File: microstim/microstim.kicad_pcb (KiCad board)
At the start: 2 copper layers, 196.1 x 76.2 mm, 97 parts, among them J1 Conn_Coaxial, J10 Conn_Coaxial, J11 Screw_Terminal_01x02, J12 Conn_Coaxial, J2 Conn_Coaxial, J3 Screw_Terminal_01x02, J4 Screw_Terminal_01x02, J5 Conn_Coaxial, J6 Conn_Coaxial, J7 Screw_Terminal_01x02, J8 Screw_Terminal_01x02, J9 Screw_Terminal_01x02, SW1 SW_Push, SW2 SW_Push, U1 Teensy3.5, U10 AD7321, U11 LTC2057, U12 LTC2057, U13 DG509ACWE, U14 DG509ACWE, U15 LT1167, U16 LT1167, U17 LM358, U18 DG509ACWE, U19 DG509ACWE, U2 CC3-0512DF-E, U3 L78L05_SO8, U4 L78L12_SO8, U5 ISO7760, U6 ISO7760, U7 ISO7341C, U8 L79L12_SO8, U9 MCP4922

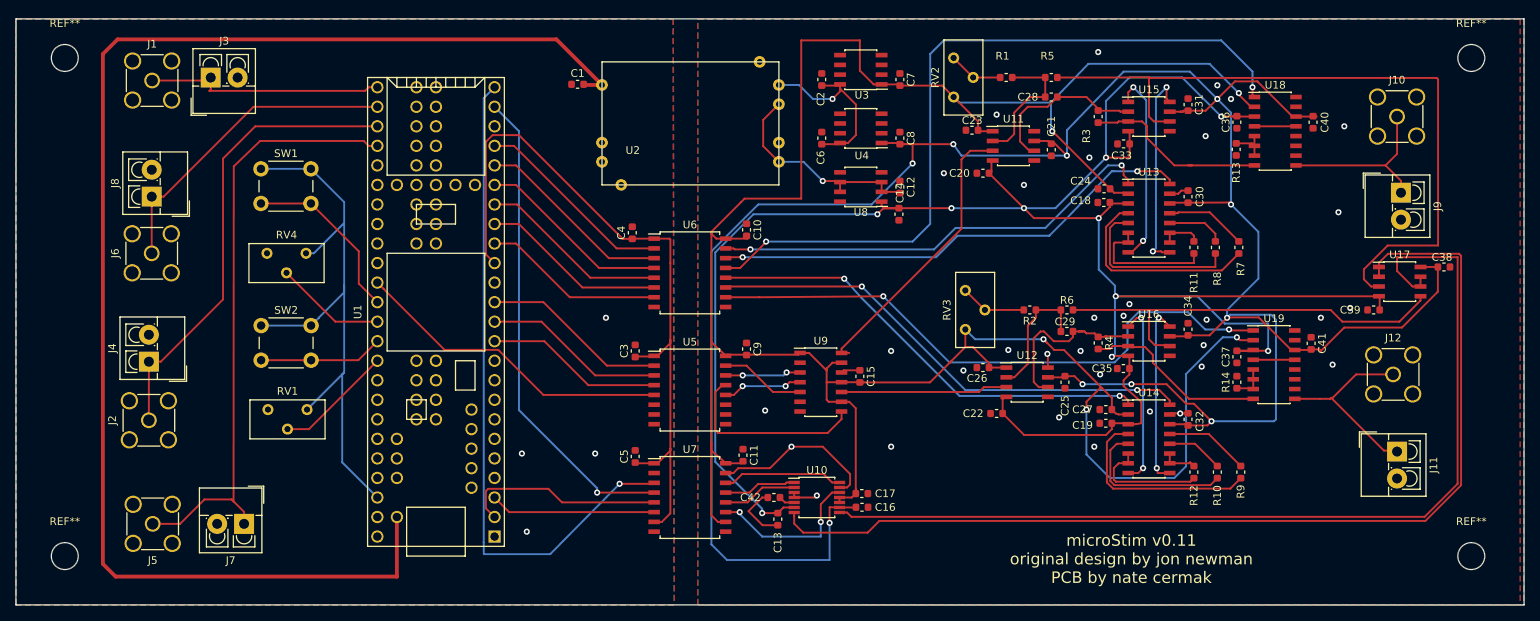
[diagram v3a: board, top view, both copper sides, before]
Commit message: redesign based on improved howland source at jon newmans suggestion
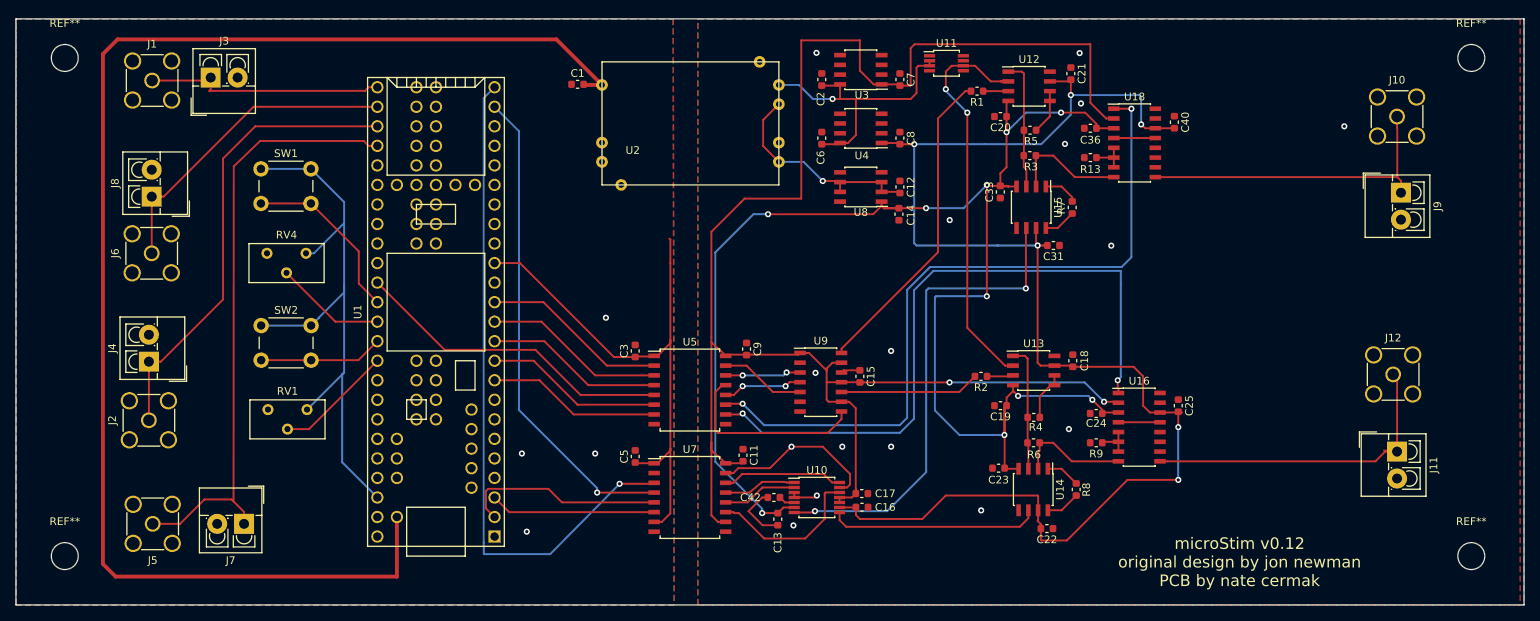
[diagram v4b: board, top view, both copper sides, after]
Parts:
- removed C10, C26, C27, C30, C32, C34, C35, C37, C38, C39, C4, C41: 0.1uF, Capacitor_SMD:C_0603_1608Metric
- removed C28, C29: 100pF, Capacitor_SMD:C_0603_1608Metric
- removed R10: 5.5k, Resistor_SMD:R_0603_1608Metric
- removed R11, R12: 50k, Resistor_SMD:R_0603_1608Metric
- removed R14: 1k, Resistor_SMD:R_0603_1608Metric
- removed RV2, RV3: 1k, Potentiometer_THT:Potentiometer_Bourns_3296Y_Vertical
- removed U17: LM358, Package_SO:SOIC-8_3.9x4.9mm_P1.27mm
- removed U19: DG509ACWE, Package_SO:SOIC-16_3.9x9.9mm_P1.27mm
- removed U6: ISO7760, Package_SO:SOIC-16W_7.5x10.3mm_P1.27mm
- R1, R2, R5: value 25k -> 3k
- R4: value 250 -> 3k
- R6: value 25k -> 250
- R7: value 1k -> 1.2k
- R8: value 5.5k -> 1.2k
- U11: value LTC2057 -> LT6657AHMS8-2.5; footprint Package_SO:SOIC-8_3.9x4.9mm_P1.27mm -> Package_SO:MSOP-8_3x3mm_P0.65mm
- U12: value LTC2057 -> AD8276
- U13: value DG509ACWE -> AD8276; footprint Package_SO:SOIC-16_3.9x9.9mm_P1.27mm -> Package_SO:SOIC-8_3.9x4.9mm_P1.27mm
- U14: value DG509ACWE -> LT1167; footprint Package_SO:SOIC-16_3.9x9.9mm_P1.27mm -> Package_SO:SOIC-8_3.9x4.9mm_P1.27mm
- U16: value LT1167 -> DG509ACWE; footprint Package_SO:SOIC-8_3.9x4.9mm_P1.27mm -> Package_SO:SOIC-16_3.9x9.9mm_P1.27mm
- moved C23 44.1 mm to (187.5, 80.0)
- moved U12 38.5 mm to (191.4, 30.4)
- moved R8 36.3 mm to (197.5, 82.8), turned to 90 degrees
- moved C24 29.2 mm to (200.2, 72.9)
- moved C31 25.3 mm to (194.6, 51.1), turned to 180 degrees
- moved U13 24.8 mm to (192.0, 67.3)
- moved R7 22.3 mm to (197.0, 46.1), turned to 90 degrees
- moved C18 21.0 mm to (197.1, 66.0), turned to 270 degrees
- moved U15 19.3 mm to (191.7, 46.1), turned to 270 degrees
- moved R9 19.2 mm to (200.2, 76.7), turned to 180 degrees
- moved C36 19.1 mm to (199.4, 35.8), turned to 0 degrees
- moved R13 19.0 mm to (199.4, 39.6), turned to 180 degrees
- moved U18 18.4 mm to (205.1, 37.7)
- moved C40 18.0 mm to (210.3, 35.0), turned to 270 degrees
- moved R6 17.8 mm to (192.0, 76.7), turned to 0 degrees
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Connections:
- C18 pad 2: -12V -> +12V
- C19 pad 1: GNDREF -> -12V
- C19 pad 2: -12V -> GNDREF
- C20 pad 1: GNDREF -> -12V
- C20 pad 2: -12V -> GNDREF
- C22 pad 2: -12V -> +12V
- C23 pad 2: +5V -> -12V
- C24 pad 2: +5V -> -12V
- R1 pad 1: Net-(C28-Pad2) -> Net-(R1-Pad1)
- R2 pad 1: Net-(C29-Pad2) -> Net-(R2-Pad1)
- R3 pad 1: Net-(C28-Pad1) -> Net-(R3-Pad1)
- R4 pad 1: Net-(C29-Pad1) -> Net-(R4-Pad1)
- R5 pad 1: Net-(R5-Pad1) -> Net-(R3-Pad1)
- R5 pad 2: Net-(C28-Pad2) -> Net-(R5-Pad2)
- R6 pad 1: Net-(R6-Pad1) -> Net-(R4-Pad1)
- R6 pad 2: Net-(C29-Pad2) -> Net-(R6-Pad2)
- R9 pad 2: Net-(R9-Pad2) -> GNDREF
- U1 pad 10: Net-(U1-Pad10) -> OE0
- U1 pad 16: OE1 -> Net-(U1-Pad16)
- U1 pad 17: GS1_1 -> Net-(U1-Pad17)
- U1 pad 18: GS1_0 -> Net-(U1-Pad18)
- U1 pad 19: OE0 -> Net-(U1-Pad19)
- U1 pad 20: GS0_1 -> Net-(U1-Pad20)
- U1 pad 21: GS0_0 -> Net-(U1-Pad21)
- U1 pad 9: Net-(U1-Pad9) -> OE1
- U11 pad 1: +5V -> Net-(U11-Pad1)
- U11 pad 2: Net-(C28-Pad2) -> +15V
- U11 pad 3: Net-(U11-Pad3) -> +15V
- U11 pad 4: -12V -> GNDREF
- U11 pad 5: (no net) -> Net-(U11-Pad5)
- U11 pad 6: Net-(C28-Pad1) -> 2.5V
- U11 pad 7: +12V -> Net-(U11-Pad7)
- U11 pad 8: GNDREF -> Net-(U11-Pad8)
- U12 pad 1: +5V -> Net-(R3-Pad1)
- U12 pad 2: Net-(C29-Pad2) -> 2.5V
- U12 pad 3: Net-(U12-Pad3) -> Net-(R1-Pad1)
- U12 pad 5: (no net) -> Net-(R5-Pad2)
- U12 pad 6: Net-(C29-Pad1) -> Net-(R5-Pad2)
- U12 pad 8: GNDREF -> Net-(U12-Pad8)
- U13 pad 1: GS0_0i -> Net-(R4-Pad1)
- U13 pad 2: +5V -> 2.5V
- U13 pad 3: -12V -> Net-(R2-Pad1)
- U13 pad 4: Net-(R7-Pad2) -> -12V
- U13 pad 5: Net-(R8-Pad2) -> Net-(R4-Pad2)
- U13 pad 6: Net-(R11-Pad2) -> Net-(R4-Pad2)
- U13 pad 7: Net-(R11-Pad2) -> +12V
- U14 pad 1: GS1_0i -> Net-(R8-Pad2)
- U14 pad 2: +5V -> Net-(R6-Pad2)
- U14 pad 3: -12V -> Net-(R4-Pad1)
- U14 pad 4: Net-(R9-Pad2) -> -12V
- U14 pad 5: Net-(R10-Pad2) -> GNDREF
- U14 pad 6: Net-(R12-Pad2) -> ISENSE1
- U14 pad 7: Net-(R12-Pad2) -> +12V
- U14 pad 8: Net-(U14-Pad8) -> Net-(R8-Pad1)
- U15 pad 1: Net-(U13-Pad8) -> Net-(R7-Pad2)
- U15 pad 3: Net-(C28-Pad1) -> Net-(R3-Pad1)
- U15 pad 6: Net-(R5-Pad1) -> ISENSE0
- U15 pad 8: Net-(U13-Pad9) -> Net-(R7-Pad1)
- U16 pad 1: Net-(U14-Pad8) -> OE1i
- U16 pad 2: Net-(R4-Pad2) -> +5V
- U16 pad 3: Net-(C29-Pad1) -> -12V
- U16 pad 4: -12V -> Net-(U16-Pad13)
- U16 pad 5: GNDREF -> Net-(R9-Pad1)
- U16 pad 6: Net-(R6-Pad1) -> Net-(R9-Pad1)
- U16 pad 7: +12V -> Net-(R9-Pad1)
- U16 pad 8: Net-(U14-Pad9) -> Net-(R6-Pad2)
- U5 pad 10: Net-(U5-Pad10) -> OE1i
- U5 pad 11: Net-(U5-Pad11) -> OE0i
- U5 pad 6: Net-(U5-Pad6) -> OE0
- U5 pad 7: Net-(U5-Pad7) -> OE1
- U9 pad 10: Net-(U12-Pad3) -> Net-(R2-Pad2)
- U9 pad 14: Net-(U11-Pad3) -> Net-(R1-Pad2)
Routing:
- net +12V: track 325.2 -> 187.8 mm, vias 10 -> 6
- net +5V: track 324.4 -> 219.2 mm, vias 5 -> 2
- net ISENSE1: track 126.7 -> 27.4 mm
- net Net-(R5-Pad1): track 93.8 -> 0.00 mm
- net -12V: track 281.8 -> 194.1 mm
- net ISENSE0: track 134.1 -> 63.9 mm, vias 0 -> 2
- net GS1_1i: track 64.5 -> 0.00 mm, vias 2 -> 0
- net GS0_1i: track 63.5 -> 0.00 mm, vias 2 -> 0
- net GS1_0i: track 59.6 -> 0.00 mm, vias 2 -> 0
- net GS0_0i: track 58.8 -> 0.00 mm, vias 2 -> 0
- net Net-(R6-Pad1): track 54.4 -> 0.00 mm
- net 2.5V: track 0.00 -> 52.8 mm, vias 0 -> 2
- net Net-(U11-Pad3): track 37.1 -> 0.00 mm
- net Net-(R1-Pad2): track 7.10 -> 41.4 mm
- net Net-(R9-Pad2): track 26.8 -> 0.00 mm
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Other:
- board text added: "microStim v0.12 original design by jon newman PCB by nate cermak"
- board text removed: "microStim v0.11 original design by jon newman PCB by nate cermak"

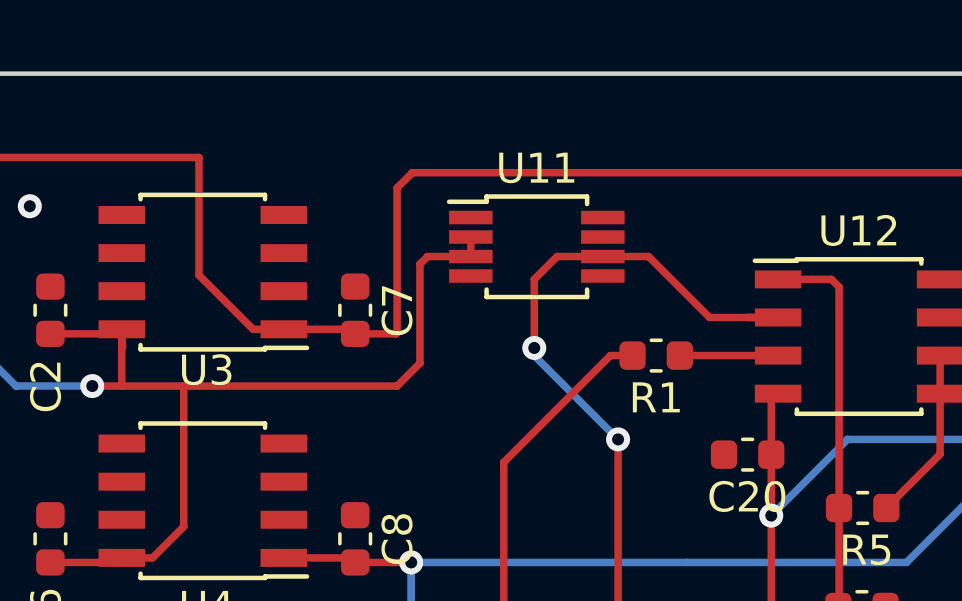
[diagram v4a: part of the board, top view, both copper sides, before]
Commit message: lots of cleanup in file structure. nearly ready to order board v0.12. need to finish BOM and commit.
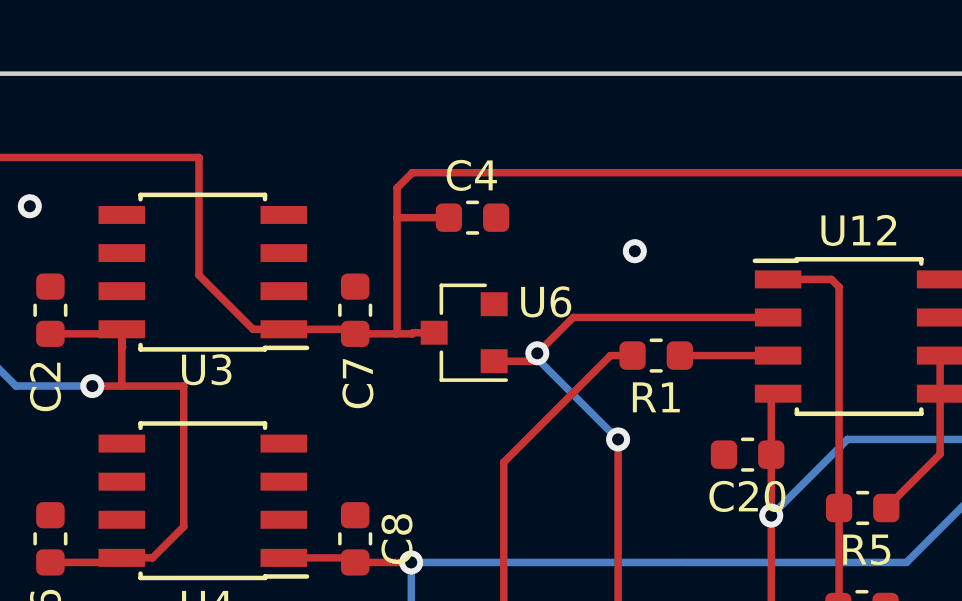
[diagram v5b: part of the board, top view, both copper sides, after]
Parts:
- removed U11: LT6657AHMS8-2.5, Package_SO:MSOP-8_3x3mm_P0.65mm
- added C4: 1uF, Capacitor_SMD:C_0603_1608Metric, F.Cu at (178.5, 26.4)
- added U6: AD1582, Package_TO_SOT_SMD:SOT-23, F.Cu at (178.3, 30.2)
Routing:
- net +15V: track 39.0 -> 25.1 mm
- net +5V: track 219.2 -> 222.2 mm
- net 2.5V: track 52.8 -> 50.3 mm
- net GNDREF: vias 16 -> 17
